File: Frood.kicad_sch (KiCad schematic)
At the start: 43 parts, among them J1 Conn_02x13+5, SW1 RESET, SW2 BOOT, U1 RP2040, U2 ZD25WQ16BUIGR, U3 SPX3819M5-L-3-3/TR, Y1 TXM12M0004252LBCEO00T

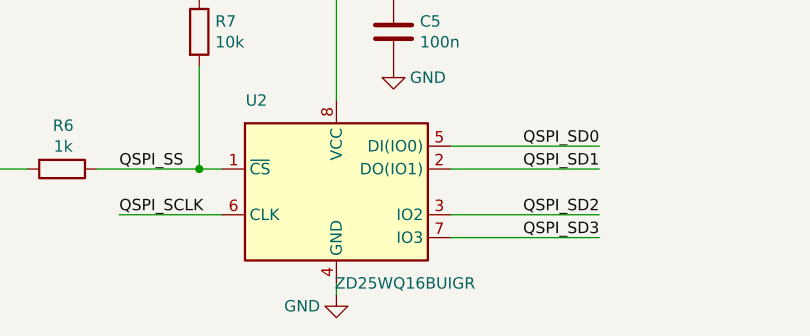
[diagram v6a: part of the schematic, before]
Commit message: Rev6 update
* Use a 4 MB (32 Mb) flash chip instead
* Minor routing fine-tuning
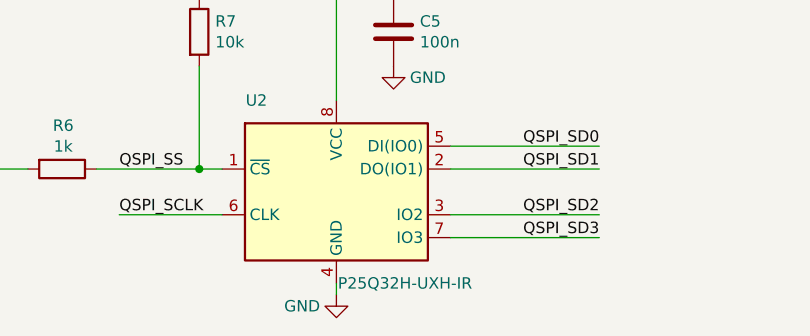
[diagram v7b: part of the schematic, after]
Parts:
- U2: value ZD25WQ16BUIGR -> P25Q32H-UXH-IR; LCSC C2759920 -> C414068
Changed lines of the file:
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@@
     (in_bom yes) (on_board yes)
     (property "Reference" "U2" (id 0) (at 161.036 244.856 0))
-    (property "Value" "ZD25WQ16BUIGR" (id 1) (at 177.546 265.176 0))
+    (property "Value" "P25Q32H-UXH-IR" (id 1) (at 177.546 265.176 0))
     (property "Footprint" "42keebs:DFN-8-1EP_3x2mm_P0.5mm_EP0.2x1.6mm" (id 2) (at 169.926 255.016 0)
       (effects (font (size 1.27 1.27)) hide)
     )
-    (property "Datasheet" "http://www.winbond.com/resource-files/w25q32jv%20revg%2003272018%20plus.pdf" (id 3) (at 169.926 255.016 0)
-      (effects (font (size 1.27 1.27)) hide)
-    )
-    (property "LCSC" "C2759920" (id 4) (at 169.926 255.016 0)
+    (property "Datasheet" "" (id 3) (at 169.926 255.016 0)
+      (effects (font (size 1.27 1.27)) hide)
+    )
+    (property "LCSC" "C414068" (id 4) (at 169.926 255.016 0)
       (effects (font (size 1.27 1.27)) hide)
     )
@@
     )
     (path "/80130354-2922-4669-916a-ca379b7dd9a6"
-      (reference "U2") (unit 1) (value "ZD25WQ16BUIGR") (footprint "42keebs:DFN-8-1EP_3x2mm_P0.5mm_EP0.2x1.6mm")
+      (reference "U2") (unit 1) (value "P25Q32H-UXH-IR") (footprint "42keebs:DFN-8-1EP_3x2mm_P0.5mm_EP0.2x1.6mm")
     )
     (path "/c779cfe3-909f-43ee-bfb4-4bb9da9ab75d"

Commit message: Rev7 update
* Use a Winbond 4 MB flash chip
* Use higher quality Panasonic reset/boot switches
* A few routing tweaks
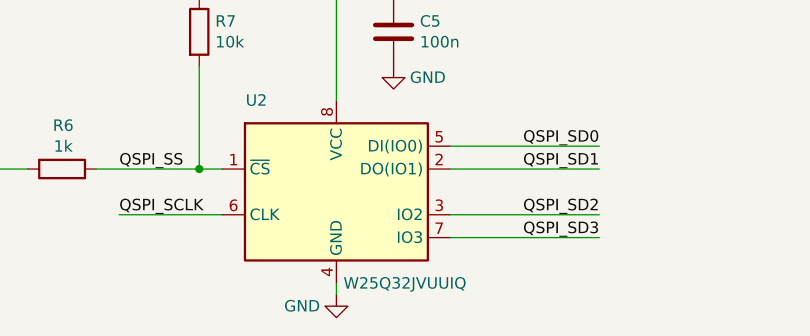
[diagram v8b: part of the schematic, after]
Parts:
- SW1, SW2: LCSC C319433 -> C2845235
- U2: value P25Q32H-UXH-IR -> W25Q32JVUUIQ; footprint 42keebs:DFN-8-1EP_3x2mm_P0.5mm_EP0.2x1.6mm -> 42keebs:USON-8_4x3mm_P0.8mm; LCSC C414068 -> C2999380
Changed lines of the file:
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@@
       (effects (font (size 1.27 1.27)) hide)
     )
-    (property "LCSC" "C319433" (id 4) (at 53.848 173.482 0)
+    (property "LCSC" "C2845235" (id 4) (at 53.848 173.482 0)
       (effects (font (size 1.27 1.27)) hide)
     )
@@
     (in_bom yes) (on_board yes)
     (property "Reference" "U2" (id 0) (at 161.036 244.856 0))
-    (property "Value" "P25Q32H-UXH-IR" (id 1) (at 177.546 265.176 0))
-    (property "Footprint" "42keebs:DFN-8-1EP_3x2mm_P0.5mm_EP0.2x1.6mm" (id 2) (at 169.926 255.016 0)
+    (property "Value" "W25Q32JVUUIQ" (id 1) (at 177.546 265.176 0))
+    (property "Footprint" "42keebs:USON-8_4x3mm_P0.8mm" (id 2) (at 169.926 255.016 0)
       (effects (font (size 1.27 1.27)) hide)
     )
@@
       (effects (font (size 1.27 1.27)) hide)
     )
-    (property "LCSC" "C414068" (id 4) (at 169.926 255.016 0)
+    (property "LCSC" "C2999380" (id 4) (at 169.926 255.016 0)
       (effects (font (size 1.27 1.27)) hide)
     )
@@
       (effects (font (size 1.27 1.27)) hide)
     )
-    (property "LCSC" "C319433" (id 4) (at 53.848 150.368 0)
+    (property "LCSC" "C2845235" (id 4) (at 53.848 150.368 0)
       (effects (font (size 1.27 1.27)) hide)
     )
@@
     )
     (path "/80130354-2922-4669-916a-ca379b7dd9a6"
-      (reference "U2") (unit 1) (value "P25Q32H-UXH-IR") (footprint "42keebs:DFN-8-1EP_3x2mm_P0.5mm_EP0.2x1.6mm")
+      (reference "U2") (unit 1) (value "W25Q32JVUUIQ") (footprint "42keebs:USON-8_4x3mm_P0.8mm")
     )
     (path "/c779cfe3-909f-43ee-bfb4-4bb9da9ab75d"
